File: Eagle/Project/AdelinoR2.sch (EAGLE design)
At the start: 80 parts, among them J1 DC-044-A, J2 YELLOW-8P-2.54, J3 YELLOW-6P-2.54, J4 YELLOW-8P-2.54, J5 YELLOW-8P-2.54, J6 4P-2.0, J7 YELLOW-2X3P-2.54, J8 4P-2.0, Q1 NCE3407A, Q2 CJ2305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

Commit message: Add DNP for 32U4 TQFP and ECC608; add some silk art for Adelino X2.
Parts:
- removed D8: BLU-0603, Seeed-LED:SMD-LED-CLEAR-BLUE(0603)
- added D2: 20V-500MA, Seeed-Diode:SMD-DIODE-SCHOTTKY-20V-500MA(SOD-123)P
- D3: value 20V-500MA -> GRE-0603; device Seeed-Diode:SMD-DIODE-SCHOTTKY-20V-500MA(SOD-123)P -> Seeed-LED:SMD-LED-CLEAR-GREEN(0603); LABEL (none) -> PWR
- D4: value GRE-0603 -> YEL-0603; device Seeed-LED:SMD-LED-CLEAR-GREEN(0603) -> Seeed-LED:SMD-LED-CLEAR-YELLOW(0603); LABEL PWR -> ACT
- D5: value YEL-0603 -> 20V-500MA; device Seeed-LED:SMD-LED-CLEAR-YELLOW(0603) -> Seeed-Diode:SMD-DIODE-SCHOTTKY-20V-500MA(SOD-123)P; LABEL ACT -> (none)
- D6: value 20V-500MA -> YEL-0603; device Seeed-Diode:SMD-DIODE-SCHOTTKY-20V-500MA(SOD-123)P -> Seeed-LED:SMD-LED-CLEAR-YELLOW(0603); LABEL (none) -> D13
- D7: value YEL-0603 -> BLU-0603; device Seeed-LED:SMD-LED-CLEAR-YELLOW(0603) -> Seeed-LED:SMD-LED-CLEAR-BLUE(0603); LABEL D13 -> WIFI
- U4: value ATMEGA32U4-MUR-QFN44 -> DNP; device Seeed-IC:MCU-ATMEGA32U4-MUR(VQFN44) -> Adelino-Misc:ATECC608(SOIC8); DESC SOCKET A - QFN44 -> ATECC608-SOIC8
- U5: value ATMEGA32U4-TQFP44 -> ATMEGA32U4-MUR-QFN44; device Seeed-IC:MCU-ATMEGA32U4-AU(TQFP44) -> Seeed-IC:MCU-ATMEGA32U4-MUR(VQFN44); DESC SOCKET B - TQFP44 -> SOCKET A - QFN44
- U6: value ATECC608-SOIC8 -> DNP; device Adelino-Misc:ATECC608(SOIC8) -> Seeed-IC:MCU-ATMEGA32U4-AU(TQFP44); DESC (none) -> SOCKET B - TQFP44
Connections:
- net +5V: now also D2.-, U4.VCC, U6.AVCC@1, U6.AVCC@2, U6.VCC@1, U6.VCC@2; no longer D3.-, U4.AVCC@1, U4.AVCC@2, U4.VCC@1, U4.VCC@2, U6.VCC
- net ACT_LED: now also U6.PD5(XCLK1/!CTS); no longer U4.PD5(XCLK1/!CTS)
- net AT_MISO: now also U6.PB3(PD0/PCINT3/MISO); no longer U4.PB3(PD0/PCINT3/MISO)
- net AT_MOSI: now also U6.PB2(PDI/PCINT2/MOSI); no longer U4.PB2(PDI/PCINT2/MOSI)
- net AT_SCK: now also U6.PB1(PCINT1/SCLK); no longer U4.PB1(PCINT1/SCLK)
- net AT_SS: now also U6.PB0(SS/PCINT0); no longer U4.PB0(SS/PCINT0)
- net D+: now also U6.D+; no longer U4.D+
- net D-: now also U6.D-; no longer U4.D-
- net ESP_EN: now also U6.PE2(!HWB); no longer U4.PE2(!HWB)
- net GND: now also D3.-, D6.-, U4.GND, U6.GND@1, U6.GND@2, U6.GND@3, U6.GND@4; no longer D5.-, D7.-, U4.GND@1, U4.GND@2, U4.GND@3, U4.GND@4, U6.GND
- net GPIO2_LED: now also D7.-; no longer D8.-
- net N$4: now also D7.+; no longer D8.+
- net PIN_A0: now also U6.PF7(ADC7/TDI); no longer U4.PF7(ADC7/TDI)
- net PIN_A1: now also U6.PF6(ADC6/TDO); no longer U4.PF6(ADC6/TDO)
- net PIN_A2: now also U6.PF5(ADC5/TMS); no longer U4.PF5(ADC5/TMS)
- net PIN_A3: now also U6.PF4(ADC4/TCK); no longer U4.PF4(ADC4/TCK)
- net PIN_A4: now also U6.PF1(ADC1); no longer U4.PF1(ADC1)
- net PIN_A5: now also U6.PF0(ADC0); no longer U4.PF0(ADC0)
- net PIN_AREF: now also U6.AREF; no longer U4.AREF
- net PIN_D0: now also U6.PD2(RXD1/INT2); no longer U4.PD2(RXD1/INT2)
- net PIN_D1: now also U6.PD3(TXD1/INT3); no longer U4.PD3(TXD1/INT3)
- net PIN_D10: now also U6.PB6(PCINT6/OC1B/OC4B/ADC13); no longer U4.PB6(PCINT6/OC1B/OC4B/ADC13)
- net PIN_D11: now also U6.PB7(PCINT7/OC0A/OC1C/!RTS); no longer U4.PB7(PCINT7/OC0A/OC1C/!RTS)
- net PIN_D12: now also U6.PD6(T1/ADC9/!OC4D); no longer U4.PD6(T1/ADC9/!OC4D)
- net PIN_D13: now also U6.PC7(ICP3/CLK0/OC4A); no longer U4.PC7(ICP3/CLK0/OC4A)
- net PIN_D2_SDA: now also U4.SDA, U6.PD1(SDA/INT1); no longer U4.PD1(SDA/INT1), U6.SDA
- net PIN_D3_SCL: now also U4.SCL, U6.PD0(OC0B/SCL/INT0); no longer U4.PD0(OC0B/SCL/INT0), U6.SCL
- net PIN_D4: now also U6.PD4(ICP1/ADC8); no longer U4.PD4(ICP1/ADC8)
- net PIN_D5: now also U6.PC6(OC3A/!OC4A); no longer U4.PC6(OC3A/!OC4A)
- net PIN_D6: now also U6.PD7(T0/OC4D/ADC10); no longer U4.PD7(T0/OC4D/ADC10)
- net PIN_D7: now also U6.PE6(INT.6/AIN0); no longer U4.PE6(INT.6/AIN0)
- net PIN_D8: now also U6.PB4(PCINT4/ADC11); no longer U4.PB4(PCINT4/ADC11)
- net PIN_D9: now also U6.PB5(PCINT5/OC1A/ADC12/!OC4B); no longer U4.PB5(PCINT5/OC1A/ADC12/!OC4B)
- net RESET: now also D2.+, U6.!RESET; no longer D3.+, U4.!RESET
- net RSTAT: now also D5.-; no longer D6.-
- net UCAP: now also U6.UCAP; no longer U4.UCAP
- net UGND: now also U6.UGND; no longer U4.UGND
- net VUSB: now also U6.UVCC, U6.VBUS; no longer U4.UVCC, U4.VBUS
- net XTAL1: now also U6.XTAL1; no longer U4.XTAL1
- net XTAL2: now also U6.XTAL2; no longer U4.XTAL2
- net _ACT: now also D4.+; no longer D6.+
- net _D13: now also D6.+; no longer D7.+
- net _PWR: now also D3.+; no longer D4.+
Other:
- moved on the sheet: C21, D4, D7, U5

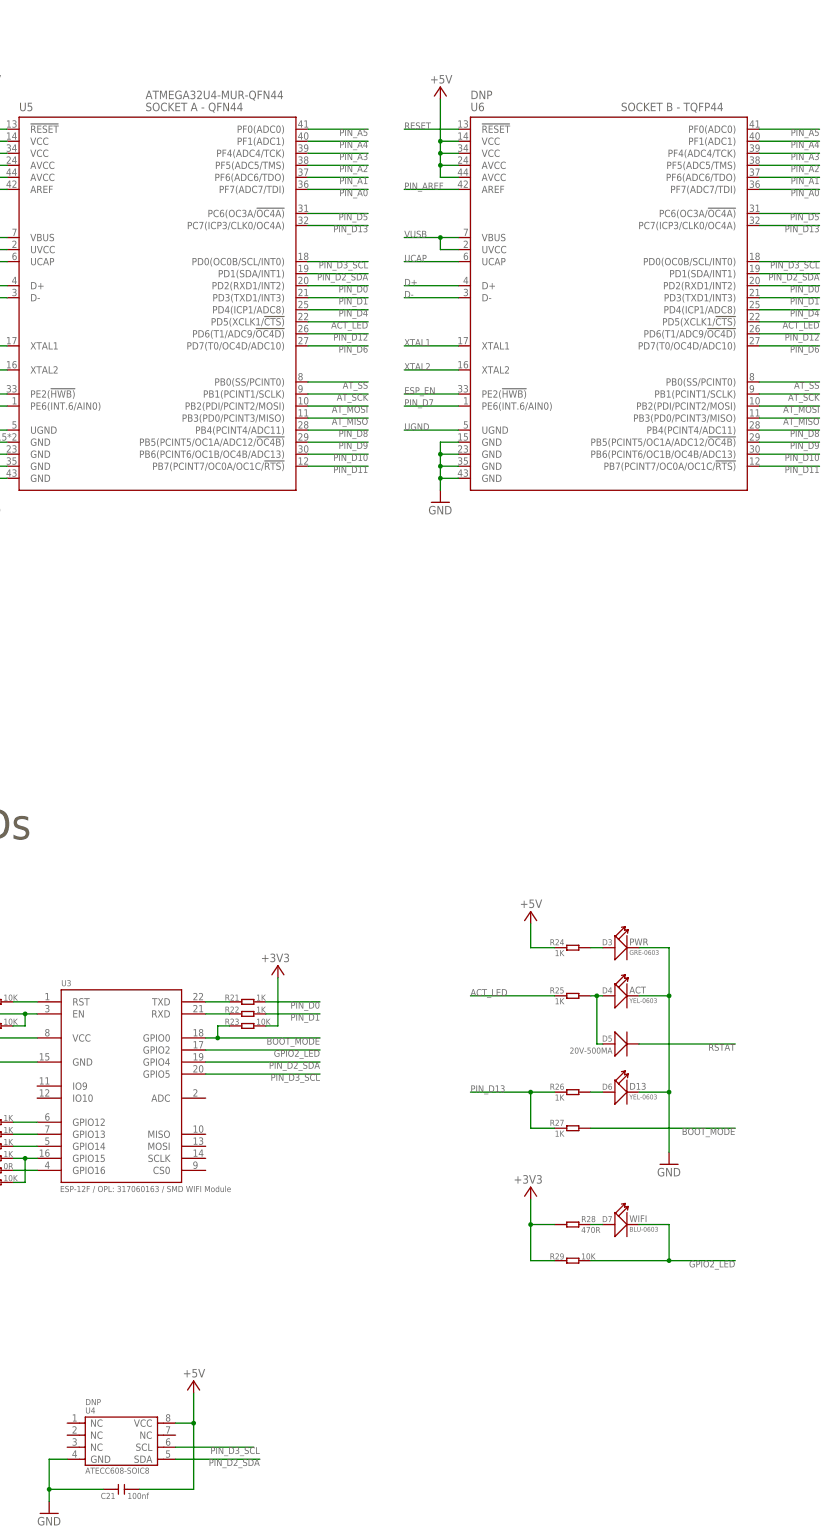
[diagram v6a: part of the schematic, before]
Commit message: Add Adelino X2 silkscreens and component position cues.
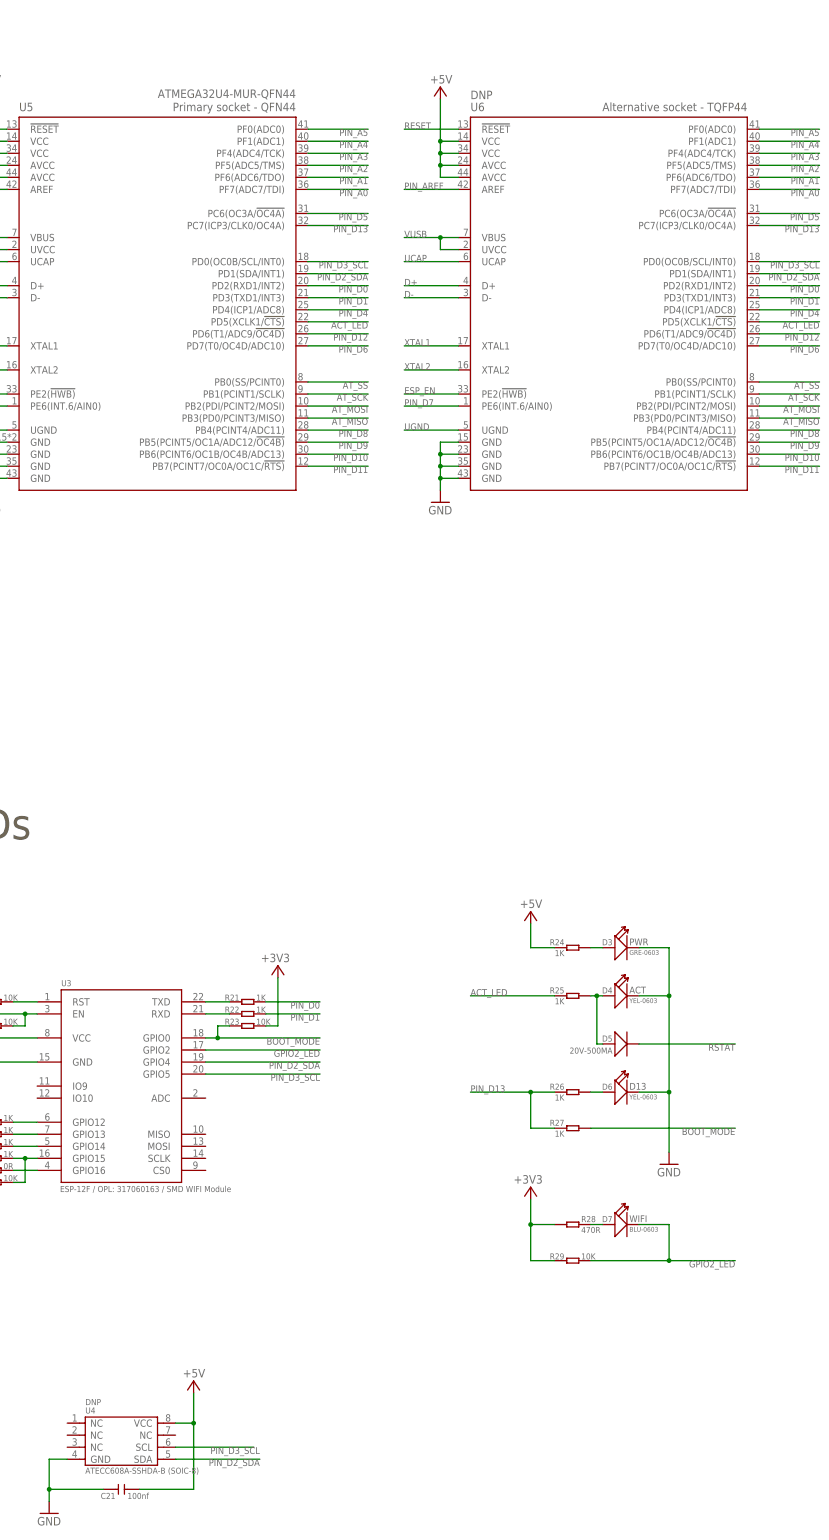
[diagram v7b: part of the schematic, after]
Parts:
- U4: DESC ATECC608-SOIC8 -> ATECC608A-SSHDA-B (SOIC-8); MOUSER_REF (none) -> https://www.mouser.com/ProductDetail/556-ATECC608ASSHDAB; MPN (none) -> ATECC608A-SSHDA-B
- U5: DESC SOCKET A - QFN44 -> Primary socket - QFN44
- U6: DESC SOCKET B - TQFP44 -> Alternative socket - TQFP44
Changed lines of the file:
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@@
 <parts>
 <part name="U5" library="Seeed-IC" deviceset="MCU-ATMEGA32U4-MUR(VQFN44)" device="" value="ATMEGA32U4-MUR-QFN44">
-<attribute name="DESC" value="SOCKET A - QFN44"/>
+<attribute name="DESC" value="Primary socket - QFN44"/>
 </part>
 <part name="U3" library="Seeed-OPL-2017-01-Sensor-camilo" deviceset="ESP-12F" device="" value="ESP-12F / OPL: 317060163 / SMD WIFI Module"/>
@@
 <part name="R5" library="Seeed-Resistor" deviceset="SMD-RES-3.3K-5%-1/16W(0402)" device="" value="3.3K"/>
 <part name="U6" library="Seeed-IC" deviceset="MCU-ATMEGA32U4-AU(TQFP44)" device="" value="DNP">
-<attribute name="DESC" value="SOCKET B - TQFP44"/>
+<attribute name="DESC" value="Alternative socket - TQFP44"/>
 </part>
 <part name="GND13" library="supply1" library_urn="urn:adsk.eagle:library:371" deviceset="GND" device=""/>
@@
 <part name="ESD1" library="Seeed-OPL-2017-01-Diode-james" deviceset="SMD-DIODE-TVS-5.5V" device="" value="PRTR5V0U2X"/>
 <part name="U4" library="Adelino-Misc" deviceset="ATECC608(SOIC8)" device="" value="DNP">
-<attribute name="DESC" value="ATECC608-SOIC8"/>
+<attribute name="DESC" value="ATECC608A-SSHDA-B (SOIC-8)"/>
+<attribute name="MOUSER_REF" value="https://www.mouser.com/ProductDetail/556-ATECC608ASSHDAB"/>
+<attribute name="MPN" value="ATECC608A-SSHDA-B"/>
 </part>
 <part name="GND12" library="supply1" library_urn="urn:adsk.eagle:library:371" deviceset="GND" device=""/>
@@
 <instance part="U5" gate="G$1" x="105.41" y="93.98" smashed="yes">
 <attribute name="NAME" x="74.93" y="133.35" size="1.778" layer="95"/>
-<attribute name="VALUE" x="101.6" y="135.89" size="1.778" layer="96"/>
-<attribute name="DESC" x="101.6" y="133.35" size="1.778" layer="96"/>
+<attribute name="VALUE" x="133.35" y="137.922" size="1.778" layer="96" rot="R180"/>
+<attribute name="DESC" x="133.35" y="135.128" size="1.778" layer="96" rot="R180"/>
 </instance>
 <instance part="U3" gate="G$1" x="96.52" y="-72.39" smashed="yes">
@@
 <attribute name="NAME" x="170.18" y="133.35" size="1.778" layer="95"/>
 <attribute name="VALUE" x="170.18" y="135.89" size="1.778" layer="96"/>
-<attribute name="DESC" x="201.93" y="133.35" size="1.778" layer="96"/>
+<attribute name="DESC" x="228.6" y="135.128" size="1.778" layer="96" rot="R180"/>
 </instance>
 <instance part="GND13" gate="1" x="163.83" y="50.8" smashed="yes">
@@
 <attribute name="VALUE" x="88.9" y="-139.7" size="1.27" layer="96" ratio="10"/>
 <attribute name="DESC" x="88.9" y="-154.178" size="1.27" layer="96"/>
+<attribute name="MOUSER_REF" x="96.52" y="-147.32" size="1.778" layer="96" display="off"/>
 </instance>
 <instance part="GND12" gate="1" x="81.28" y="-162.56" smashed="yes">
